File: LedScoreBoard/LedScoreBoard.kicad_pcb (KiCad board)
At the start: 2 copper layers, 149.9 x 149.9 mm, 115 parts, among them J101 LCD, J102 1, J103 10, J104 100, J105 DC12_IN, J106 VDD_IN, J107 PICkit, J108 TweLite-R, Q201 BSS138, Q202 BSS84, Q203 BSS138, Q204 2SJ349, Q205 BSS138, Q206 BSS84, Q207 BSS138, Q208 2SJ349, Q209 BSS138, Q210 BSS84, Q211 BSS138, Q212 2SJ349, Q301 BSS138, Q302 TK40E06N1, Q303 BSS138, Q304 TK40E06N1, Q305 BSS138, Q306 TK40E06N1, Q307 BSS138, Q308 TK40E06N1, Q309 BSS138, Q310 TK40E06N1, Q311 BSS138, Q312 TK40E06N1, Q313 BSS138, Q314 TK40E06N1, SW101 SW_Push, SW102 PlusHun, SW103 MinusHun, SW104 PlusTen, SW105 MinusTen, SW106 PlusOne, SW107 MinusOne, U101 PIC16F1516-ISP, U102 MW-R-WX, U103 LM2931-3.3_TO220, U301 LM358, U302 LM358, U303 LM358, U304 LM358

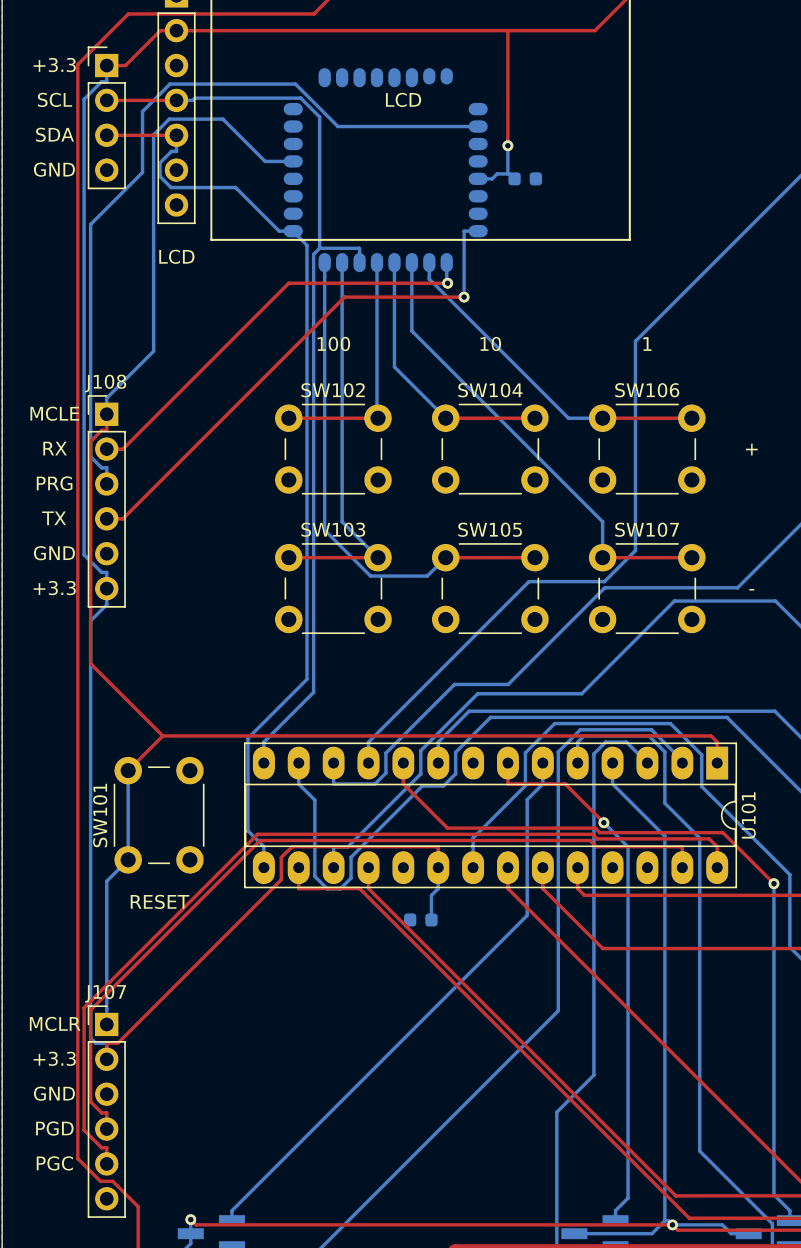
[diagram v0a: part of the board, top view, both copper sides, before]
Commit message: PIC/Twelite書き込み端子ネットリスト修正
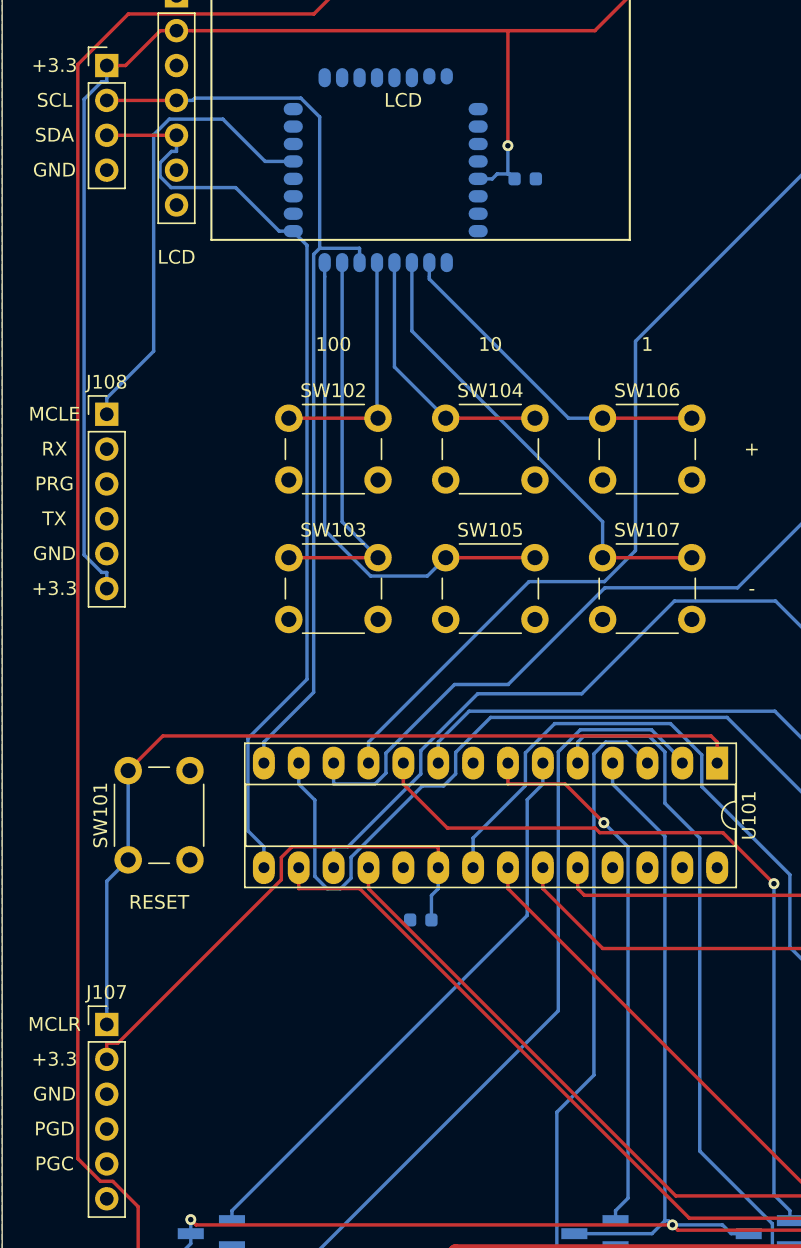
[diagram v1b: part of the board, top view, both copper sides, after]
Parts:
- U101: value PIC16F1516-ISP -> PIC16F1783
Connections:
- J108 pad 1: /MCLR -> GND
- J108 pad 2: /RX -> /TX
- J108 pad 4: /TX -> /RX
- J108 pad 5: GND -> /MCLR
- U101 pad 27: /PGD -> /PGC
- U101 pad 28: /PGC -> /PGD
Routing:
- net /PGC: track 65.5 -> 0.00 mm
- net /PGD: track 59.3 -> 0.00 mm
- net /PRG: track 56.0 -> 0.00 mm
- net /TX: track 38.5 -> 0.00 mm, vias 1 -> 0
- net +3.3V: track 193.9 -> 158.2 mm
- net /RX: track 31.4 -> 0.00 mm, vias 1 -> 0
- net /MCLR: track 124.8 -> 98.5 mm

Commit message: Vref修正
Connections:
- Q301 pad 3: /Vref -> /LedCathodeDrivers/Vref
- Q303 pad 3: /Vref -> /LedCathodeDrivers/Vref
- Q305 pad 3: /Vref -> /LedCathodeDrivers/Vref
- Q307 pad 3: /Vref -> /LedCathodeDrivers/Vref
- Q309 pad 3: /Vref -> /LedCathodeDrivers/Vref
- Q311 pad 3: /Vref -> /LedCathodeDrivers/Vref
- Q313 pad 3: /Vref -> /LedCathodeDrivers/Vref
- U301 pad 1: /Vref -> /LedCathodeDrivers/Vref
- U301 pad 2: /Vref -> /LedCathodeDrivers/Vref
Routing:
- net /Vref: track 190.5 -> 0.00 mm, vias 3 -> 0
- net /MCLR: track 98.5 -> 64.8 mm
- net GND: track 0.00 -> 33.7 mm

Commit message: 回路修正
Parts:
- removed REF01, REF02, REF03, REF04: MountingHole_3.2mm_M3, MountingHole:MountingHole_3.2mm_M3
- removed REF05: MountingHole_6.4mm_M6, MountingHole:MountingHole_6.4mm_M6
- removed REF06, REF07, REF08, REF09, REF10, REF11, REF12, REF13, REF14, REF15: MountingHole_2.2mm_M2, MountingHole:MountingHole_2.2mm_M2
- added R101: 10k, Resistor_SMD:R_0603_1608Metric, F.Cu at (-179.3, 113.7)
- added R322: 20, Resistor_SMD:R_0603_1608Metric, F.Cu at (-61.7, 90.8)
- added R323: 1k, Resistor_SMD:R_0603_1608Metric, F.Cu at (-57.6, 90.8)
- added R324: 1.0, Resistor_SMD:R_2512_6332Metric_Pad1.40x3.35mm_HandSolder, F.Cu at (-99.7, 109.7)
- added R325: 10k, Resistor_SMD:R_0603_1608Metric, F.Cu at (-80.7, 110.8)
- added R326: 20, Resistor_SMD:R_0603_1608Metric, F.Cu at (-98.2, 113.4)
- added R327: 1k, Resistor_SMD:R_0603_1608Metric, F.Cu at (-80.7, 113.3)
- added R328: 1.0, Resistor_SMD:R_2512_6332Metric_Pad1.40x3.35mm_HandSolder, F.Cu at (-88.2, 92.9)
- added SW108: MinusOne, Button_Switch_THT:SW_PUSH_6mm, F.Cu at (-152.9, 100.2)
- C101, C102, C103, C104, C201, C301, C302, C303, C304, C305, C306, C307, C308, C309, C310, C311, D201, Q201, Q202, Q203, Q205, Q206, Q207, Q209, Q210, Q211, Q301, Q303, Q305, Q307, Q309, Q311, Q313, R201, R202, R203, R204, R205, R206, R207, R208, R209, R210, R310, R311, R312, U102: moved to F.Cu
- D202, D203, D204: footprint Diode_THT:D_DO-27_P12.70mm_Horizontal -> Diode_THT:D_DO-27_P15.24mm_Horizontal; moved to F.Cu
- J101: value LCD -> TweLite-R; footprint Connector_PinSocket_2.54mm:PinSocket_1x07_P2.54mm_Vertical -> Connector_PinHeader_2.54mm:PinHeader_1x06_P2.54mm_Vertical
- J102: value 1 -> LCD; footprint Connector_JST:JST_VH_B8P-VH_1x08_P3.96mm_Vertical -> Connector_PinSocket_2.54mm:PinSocket_1x07_P2.54mm_Vertical
- J103: value 10 -> PICkit; footprint Connector_JST:JST_VH_B8P-VH_1x08_P3.96mm_Vertical -> Connector_PinHeader_2.54mm:PinHeader_1x06_P2.54mm_Vertical
- J104: value 100 -> 1
- J105: value DC12_IN -> 10; footprint TerminalBlock:TerminalBlock_bornier-2_P5.08mm -> Connector_JST:JST_VH_B8P-VH_1x08_P3.96mm_Vertical
- J106: value VDD_IN -> 100; footprint TerminalBlock:TerminalBlock_bornier-2_P5.08mm -> Connector_JST:JST_VH_B8P-VH_1x08_P3.96mm_Vertical
- J107: value PICkit -> DC12_IN; footprint Connector_PinHeader_2.54mm:PinHeader_1x06_P2.54mm_Vertical -> TerminalBlock:TerminalBlock_bornier-2_P5.08mm
- J108: value TweLite-R -> VDD_IN; footprint Connector_PinHeader_2.54mm:PinHeader_1x06_P2.54mm_Vertical -> TerminalBlock:TerminalBlock_bornier-2_P5.08mm
- R301, R313: value 20 -> 10k; moved to F.Cu
- R302, R314: value 1k -> 20; moved to F.Cu
- R303, R315: value 1.0 -> 1k; footprint Resistor_SMD:R_2512_6332Metric_Pad1.40x3.35mm_HandSolder -> Resistor_SMD:R_0603_1608Metric; moved to F.Cu
- R304, R316: value 20 -> 1.0; footprint Resistor_SMD:R_0603_1608Metric -> Resistor_SMD:R_2512_6332Metric_Pad1.40x3.35mm_HandSolder; moved to F.Cu
- R305, R317: value 1k -> 10k; moved to F.Cu
- R306, R318: value 1.0 -> 20; footprint Resistor_SMD:R_2512_6332Metric_Pad1.40x3.35mm_HandSolder -> Resistor_SMD:R_0603_1608Metric; moved to F.Cu
- R307, R319: value 20 -> 1k; moved to F.Cu
- R308, R320: value 1k -> 1.0; footprint Resistor_SMD:R_0603_1608Metric -> Resistor_SMD:R_2512_6332Metric_Pad1.40x3.35mm_HandSolder; moved to F.Cu
- R309, R321: value 1.0 -> 10k; footprint Resistor_SMD:R_2512_6332Metric_Pad1.40x3.35mm_HandSolder -> Resistor_SMD:R_0603_1608Metric; moved to F.Cu
- SW102: value PlusHun -> SW_Push
- SW103: value MinusHun -> PlusHun
- SW104: value PlusTen -> MinusHun
- SW105: value MinusTen -> PlusTen
- SW106: value PlusOne -> MinusTen
- SW107: value MinusOne -> PlusOne
- U301, U302, U303, U304: footprint Package_SO:TSSOP-8_3x3mm_P0.65mm -> Package_SO:SOP-8_3.9x4.9mm_P1.27mm; moved to F.Cu
- moved J102 321.7 mm to (-182.9, 91.4)
- moved J103 310.3 mm to (-173.7, 91.4)
- moved J106 302.9 mm to (-181.9, 83.3)
- moved C104 290.5 mm to (-195.0, 127.7), turned to 0 degrees
- moved J104 284.6 mm to (-147.7, 83.3)
- moved Q314 271.5 mm to (-101.0, 100.4), turned to 0 degrees
- moved C103 270.2 mm to (-183.3, 113.7)
- moved J105 269.2 mm to (-193.6, 120.6)
- moved U101 268.4 mm to (-194.9, 80.7), turned to 0 degrees
- moved U103 265.2 mm to (-177.4, 110.4)
- moved Q312 254.8 mm to (-101.0, 88.4), turned to 0 degrees
- moved R316 248.6 mm to (-99.7, 104.8), turned to 0 degrees
- moved C102 246.5 mm to (-183.3, 110.2), turned to 0 degrees
- moved C101 242.1 mm to (-191.0, 127.7)
- moved R320 241.8 mm to (-76.6, 87.0)
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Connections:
- J101 pad 1: unconnected-(J101-Pad1) -> GND
- J101 pad 2: +3.3V -> /TX
- J101 pad 3: /RST -> /PRG
- J101 pad 4: /SCL -> /RX
- J101 pad 5: /SDA -> /RESET
- J101 pad 6: GND -> +3.3V
- J102 pad 1: /LedAnodeDrivers/AnodeOne -> unconnected-(J102-Pad1)
- J102 pad 2: /LedCathodeDrivers/CathodeA -> +3.3V
- J102 pad 3: /LedCathodeDrivers/CathodeB -> Net-(J102-Pad3)
- J102 pad 4: /LedCathodeDrivers/CathodeC -> /SCL
- J102 pad 5: /LedCathodeDrivers/CathodeD -> /SDA
- J102 pad 6: /LedCathodeDrivers/CathodeE -> GND
- J102 pad 7: /LedCathodeDrivers/CathodeF -> unconnected-(J102-Pad7)
- J103 pad 1: /LedAnodeDrivers/AnodeTen -> /MCLR
- J103 pad 2: /LedCathodeDrivers/CathodeA -> +3.3V
- J103 pad 3: /LedCathodeDrivers/CathodeB -> GND
- J103 pad 4: /LedCathodeDrivers/CathodeC -> /PGD
- J103 pad 5: /LedCathodeDrivers/CathodeD -> /PGC
- J103 pad 6: /LedCathodeDrivers/CathodeE -> unconnected-(J103-Pad6)
- J104 pad 1: /LedAnodeDrivers/AnodeHun -> /LedAnodeDrivers/AnodeOne
- J105 pad 1: +12V -> /LedAnodeDrivers/AnodeTen
- J105 pad 2: GND -> /LedCathodeDrivers/CathodeA
- J106 pad 1: VDD -> /LedAnodeDrivers/AnodeHun
- J106 pad 2: GND -> /LedCathodeDrivers/CathodeA
- J107 pad 1: /MCLR -> +12V
- J107 pad 2: +3.3V -> GND
- J108 pad 1: GND -> VDD
- J108 pad 2: /TX -> GND
- R301 pad 1: Net-(R301-Pad1) -> Net-(Q301-Pad2)
- R301 pad 2: Net-(Q302-Pad1) -> GND
- R302 pad 1: /CsensA -> Net-(R302-Pad1)
- R302 pad 2: Net-(Q302-Pad3) -> Net-(Q302-Pad1)
- R303 pad 1: Net-(Q302-Pad3) -> /CsensA
- R303 pad 2: GND -> Net-(Q302-Pad3)
- R304 pad 1: Net-(R304-Pad1) -> Net-(Q302-Pad3)
- R304 pad 2: Net-(Q304-Pad1) -> GND
- R305 pad 1: /CsensB -> Net-(Q303-Pad2)
- R305 pad 2: Net-(Q304-Pad3) -> GND
- R306 pad 1: Net-(Q304-Pad3) -> Net-(R306-Pad1)
- R306 pad 2: GND -> Net-(Q304-Pad1)
- R307 pad 1: Net-(R307-Pad1) -> /CsensB
- R307 pad 2: Net-(Q306-Pad1) -> Net-(Q304-Pad3)
- R308 pad 1: /CsensC -> Net-(Q304-Pad3)
- R308 pad 2: Net-(Q306-Pad3) -> GND
- R309 pad 1: Net-(Q306-Pad3) -> Net-(Q305-Pad2)
- R310 pad 2: Net-(Q308-Pad1) -> Net-(Q306-Pad1)
- R311 pad 1: /CsensD -> /CsensC
- R311 pad 2: Net-(Q308-Pad3) -> Net-(Q306-Pad3)
- R312 pad 1: Net-(Q308-Pad3) -> Net-(Q306-Pad3)
- R313 pad 1: Net-(R313-Pad1) -> Net-(Q307-Pad2)
- R313 pad 2: Net-(Q310-Pad1) -> GND
- R314 pad 1: /CsensE -> Net-(R314-Pad1)
- R314 pad 2: Net-(Q310-Pad3) -> Net-(Q308-Pad1)
- R315 pad 1: Net-(Q310-Pad3) -> /CsensD
- R315 pad 2: GND -> Net-(Q308-Pad3)
- R316 pad 1: Net-(R316-Pad1) -> Net-(Q308-Pad3)
- R316 pad 2: Net-(Q312-Pad1) -> GND
- R317 pad 1: /CsensF -> Net-(Q309-Pad2)
- R317 pad 2: Net-(Q312-Pad3) -> GND
- R318 pad 1: Net-(Q312-Pad3) -> Net-(R318-Pad1)
- R318 pad 2: GND -> Net-(Q310-Pad1)
- R319 pad 1: Net-(R319-Pad1) -> /CsensE
- R319 pad 2: Net-(Q314-Pad1) -> Net-(Q310-Pad3)
- R320 pad 1: /CsensG -> Net-(Q310-Pad3)
- R320 pad 2: Net-(Q314-Pad3) -> GND
- R321 pad 1: Net-(Q314-Pad3) -> Net-(Q311-Pad2)
- SW102 pad 1: /PlusHun -> /RESET
- SW103 pad 1: /MinusHun -> /PlusHun
- SW104 pad 1: /PlusTen -> /MinusHun
- SW105 pad 1: /MinusTen -> /PlusTen
- SW106 pad 1: /PlusOne -> /MinusTen
- SW107 pad 1: /MinusOne -> /PlusOne
- U102 pad 21: /MCLR -> /RESET
- U301 pad 7: Net-(R301-Pad1) -> Net-(R302-Pad1)
- U302 pad 1: Net-(R304-Pad1) -> Net-(R306-Pad1)
- U302 pad 7: Net-(R307-Pad1) -> Net-(R310-Pad1)
- U303 pad 1: Net-(R310-Pad1) -> Net-(R314-Pad1)
- U303 pad 7: Net-(R313-Pad1) -> Net-(R318-Pad1)
- U304 pad 1: Net-(R316-Pad1) -> Net-(R322-Pad1)
- U304 pad 7: Net-(R319-Pad1) -> Net-(R326-Pad1)
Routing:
- net +12V: track 329.9 -> 0.00 mm, vias 4 -> 0
- net VDD: track 258.6 -> 0.00 mm
- net /LedCathodeDrivers/CathodeA: track 205.4 -> 0.00 mm
- net /LedCathodeDrivers/CathodeB: track 190.3 -> 0.00 mm
- net /LedCathodeDrivers/CathodeC: track 176.1 -> 0.00 mm
- net /LedCathodeDrivers/CathodeD: track 162.3 -> 0.00 mm
- net +3.3V: track 158.2 -> 0.00 mm, vias 1 -> 0
- net /LedCathodeDrivers/CathodeE: track 148.4 -> 0.00 mm
- net /LedCathodeDrivers/CathodeF: track 134.2 -> 0.00 mm
- net /SegmentF: track 130.4 -> 0.00 mm
- net /CsensG: track 127.4 -> 0.00 mm, vias 1 -> 0
- net /SegmentG: track 126.3 -> 0.00 mm, vias 1 -> 0
- net /LedCathodeDrivers/CathodeG: track 118.7 -> 0.00 mm
- net /CsensF: track 107.0 -> 0.00 mm, vias 1 -> 0
- net /SegmentE: track 88.3 -> 0.00 mm, vias 1 -> 0
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- removed copper zone on B.Cu, net GND
- removed copper zone on F.Cu, net GND
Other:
- board text removed: "+"
- board text removed: "+12"
- board text removed: "+3.3"
- board text removed: "-"
- board text removed: "1"
- board text removed: "10"
- board text removed: "100"
- board text removed: "A B C D E F G"
- board text removed: "GND"
- board text removed: "LCD"
- board text removed: "MCLE"
- board text removed: "MCLR"
- board text removed: "PGC"
- board text removed: "PGD"
- board text removed: "PRG"
- board text removed: "RESET"
- board text removed: "RX"
- board text removed: "SCL"
- board text removed: "SDA"
- board text removed: "TX"
- board text removed: "VDD"

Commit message: ver2完成
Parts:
- added G***: LOGO, image:logo, B.Cu at (94.0, 168.9)
- added H101: MountingHole, MountingHole:MountingHole_3.2mm_M3, F.Cu at (25.4, 30.5)
- added H102: MountingHole, MountingHole:MountingHole_3.2mm_M3, F.Cu at (165.1, 30.5)
- added H103: MountingHole, MountingHole:MountingHole_3.2mm_M3, F.Cu at (25.4, 170.2)
- added H104: MountingHole, MountingHole:MountingHole_3.2mm_M3, F.Cu at (165.1, 170.2)
- added H105: MountingHole, MountingHole:MountingHole_6.4mm_M6, F.Cu at (38.1, 35.6)
- added H201: MountingHole, MountingHole:MountingHole_2.2mm_M2, F.Cu at (109.2, 57.1)
- added H202: MountingHole, MountingHole:MountingHole_2.2mm_M2, F.Cu at (109.2, 82.5)
- added H203: MountingHole, MountingHole:MountingHole_2.2mm_M2, F.Cu at (109.2, 108.0)
- added H301: MountingHole, MountingHole:MountingHole_2.2mm_M2, F.Cu at (33.0, 161.3)
- added H302: MountingHole, MountingHole:MountingHole_2.2mm_M2, F.Cu at (53.3, 161.3)
- added H303: MountingHole, MountingHole:MountingHole_2.2mm_M2, F.Cu at (73.7, 161.3)
- added H304: MountingHole, MountingHole:MountingHole_2.2mm_M2, F.Cu at (94.0, 161.3)
- added H305: MountingHole, MountingHole:MountingHole_2.2mm_M2, F.Cu at (114.3, 161.3)
- added H306: MountingHole, MountingHole:MountingHole_2.2mm_M2, F.Cu at (134.6, 161.3)
- added H307: MountingHole, MountingHole:MountingHole_2.2mm_M2, F.Cu at (154.9, 161.3)
- added R102: 15k, Resistor_SMD:R_0603_1608Metric, B.Cu at (47.0, 113.0)
- added R103: 680, Resistor_SMD:R_0603_1608Metric, B.Cu at (47.0, 115.6)
- added R104: 10k, Resistor_SMD:R_0603_1608Metric, B.Cu at (40.6, 63.5)
- added R105: 10k, Resistor_SMD:R_0603_1608Metric, B.Cu at (40.6, 61.0)
- C101, C102, C103, C104, C201, C301, C302, C303, C304, C305, C306, C307, C308, C309, C310, C311, D201, D202, D203, D204, Q201, Q202, Q203, Q204, Q205, Q206, Q207, Q208, Q209, Q210, Q211, Q212, Q301, Q302, Q303, Q304, Q305, Q306, Q307, Q308, Q309, Q310, Q311, Q312, Q313, Q314, R101, R201, R202, R203, R204, R205, R206, R207, R208, R209, R210, R301, R302, R303, R304, R305, R306, R307, R308, R309, R310, R311, R312, R313, R314, R315, R316, R317, R318, R319, R320, R321, R322, R323, R324, R325, R326, R327, R328, U101, U102, U103, U301, U302, U303, U304: moved to B.Cu
- J101: footprint Connector_PinHeader_2.54mm:PinHeader_1x06_P2.54mm_Vertical -> Connector_PinSocket_2.54mm:PinSocket_1x06_P2.54mm_Horizontal
- J103: footprint Connector_PinHeader_2.54mm:PinHeader_1x06_P2.54mm_Vertical -> Connector_PinHeader_2.54mm:PinHeader_1x06_P2.54mm_Horizontal
- J107: value DC12_IN -> Conn_01x03_Male; footprint TerminalBlock:TerminalBlock_bornier-2_P5.08mm -> Connector_JST:JST_VH_B3P-VH_1x03_P3.96mm_Vertical
- J108: value VDD_IN -> Conn_01x02_Male; footprint TerminalBlock:TerminalBlock_bornier-2_P5.08mm -> Connector_PinHeader_2.54mm:PinHeader_1x02_P2.54mm_Vertical
- moved J105 328.7 mm to (132.1, 76.2)
- moved J106 314.5 mm to (132.1, 101.6)
- moved J104 281.7 mm to (132.1, 50.8)
- moved C103 275.8 mm to (81.3, 35.6)
- moved C104 272.0 mm to (61.0, 35.6), turned to 180 degrees
- moved U103 262.0 mm to (73.7, 35.6), turned to 180 degrees
- moved Q314 259.2 mm to (152.4, 154.9)
- moved J107 259.1 mm to (111.8, 33.0)
- moved R328 259.1 mm to (165.1, 147.3), turned to 90 degrees
- moved C102 254.1 mm to (66.0, 61.0), turned to -90 degrees
- moved C101 253.7 mm to (62.2, 113.0), turned to 180 degrees
- moved R326 252.0 mm to (152.4, 139.7)
- moved R324 247.4 mm to (144.8, 147.3), turned to 90 degrees
- moved Q312 242.4 mm to (132.1, 154.9)
- moved D202 242.2 mm to (124.5, 43.2), turned to 180 degrees
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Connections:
- net /Vref renamed /PicVref
- J101 pad 6: +3.3V -> Net-(J101-Pad6)
- J103 pad 1: /MCLR -> unconnected-(J103-Pad1)
- J103 pad 2: +3.3V -> /PGC
- J103 pad 3: GND -> /PGD
- J103 pad 4: /PGD -> GND
- J103 pad 5: /PGC -> +3.3V
- J103 pad 6: unconnected-(J103-Pad6) -> /MCLR
- J107 pad 2: GND -> VDD
- J108 pad 1: VDD -> Net-(J101-Pad6)
- J108 pad 2: GND -> +3.3V
- U101 pad 25: unconnected-(U101-Pad25) -> Net-(U101-Pad25)
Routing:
- net VDD: track 0.00 -> 347.7 mm, vias 0 -> 1
- net +12V: track 0.00 -> 333.7 mm, vias 0 -> 5
- net +3.3V: track 0.00 -> 203.2 mm
- net /LedCathodeDrivers/CathodeA: track 0.00 -> 190.0 mm
- net /LedCathodeDrivers/Vref: track 0.00 -> 178.5 mm, vias 0 -> 3
- net /LedCathodeDrivers/CathodeB: track 0.00 -> 174.3 mm
- net /LedCathodeDrivers/CathodeC: track 0.00 -> 158.6 mm
- net /LedCathodeDrivers/CathodeD: track 0.00 -> 142.8 mm
- net /CsensG: track 0.00 -> 131.9 mm, vias 0 -> 1
- net /LedCathodeDrivers/CathodeE: track 0.00 -> 127.1 mm
- net /LedCathodeDrivers/CathodeF: track 0.00 -> 112.9 mm
- net /LedCathodeDrivers/CathodeG: track 0.00 -> 106.2 mm
- net /CsensF: track 0.00 -> 106.1 mm, vias 0 -> 1
- net /SegmentG: track 0.00 -> 94.2 mm, vias 0 -> 1
- net /SegmentF: track 0.00 -> 93.3 mm
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- added copper zone on B.Cu, net GND
- added copper zone on F.Cu, net GND
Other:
- board text added: "+"
- board text added: "-"
- board text added: "1"
- board text added: "10"
- board text added: "100"
- board text added: "RST"
